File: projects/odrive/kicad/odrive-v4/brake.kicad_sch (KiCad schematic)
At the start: 29 parts, among them J13 BRAKE_EXT, Q50 NVMFS5C628NL/BSC027N10NS5, Q51 NVMFS5C628NL/BSC027N10NS5, U50 UCC27517A, U51 INA181A2, U52 TLV7031, U53 74LVC1G74, U54 74LVC1G32, U55 74LVC1G08

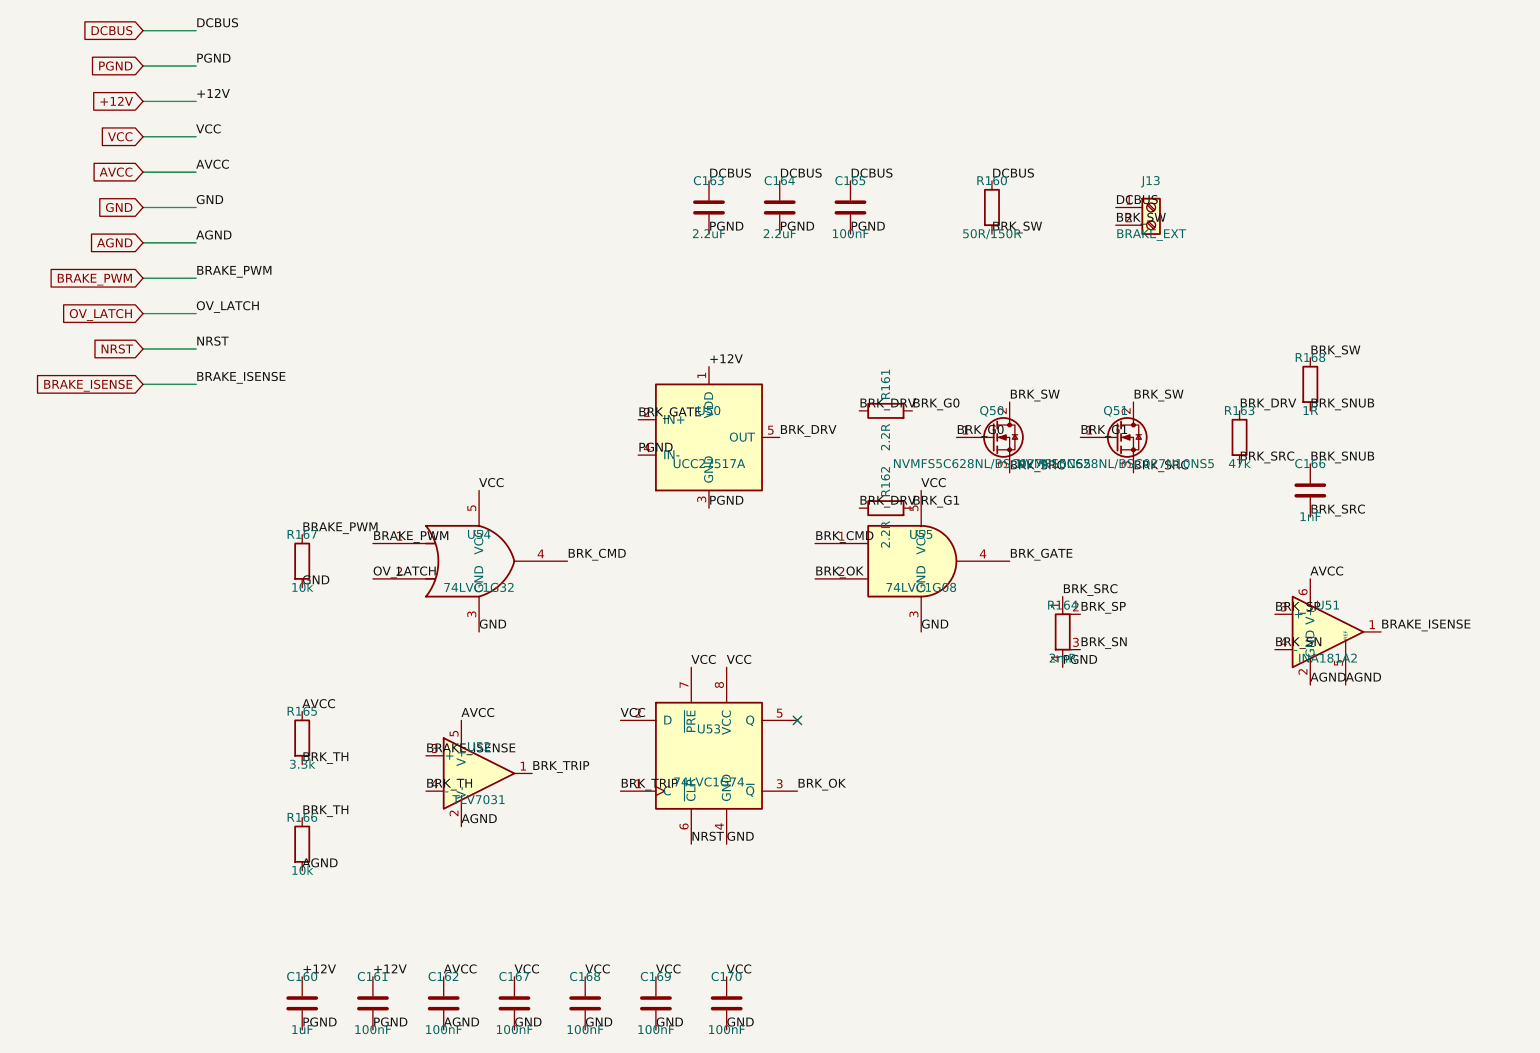
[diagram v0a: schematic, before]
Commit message: Make the v4 schematic sheets readable, netlist-invariant
The verified v4 schematic was electrically perfect and visually unreadable:
connectivity lived in labels stuck on pins, text overlapped, and parts sat
on the title block. Reworked all ten block sheets through Konnect: real
wires for local connections, labels kept for power rails and inter-sheet
nets, parts grouped by function, junction dots where wires join.

The invariant was enforced, not assumed: the exported netlist is diffed
against a reference frozen before the rework - 378 components and 283 nets,
identical membership pin by pin - and ERC holds at 0 errors. The lesson
that forced the rework is now a standing gate: numeric oracles (ERC,
netlist diff, overlap counts) all passed on the unreadable version, so
every sheet is also rendered to PNG and looked at before being declared
done.

An interrupted fix round left one known cosmetic issue, documented in
docs/LOG.md: the encoders-gpio GPIO group's reference/value text fields
float ~134mm right of their symbols, over the title block. konnect 0.2.2
has no tool that repositions property fields, so it waits for 0.11.0.
Also adds the fab footprints the sheets reference (MEGA fuse, Phoenix
terminal blocks, CMC) and restores the board file to the blank template -
the aborted layout skeleton was not worth keeping.
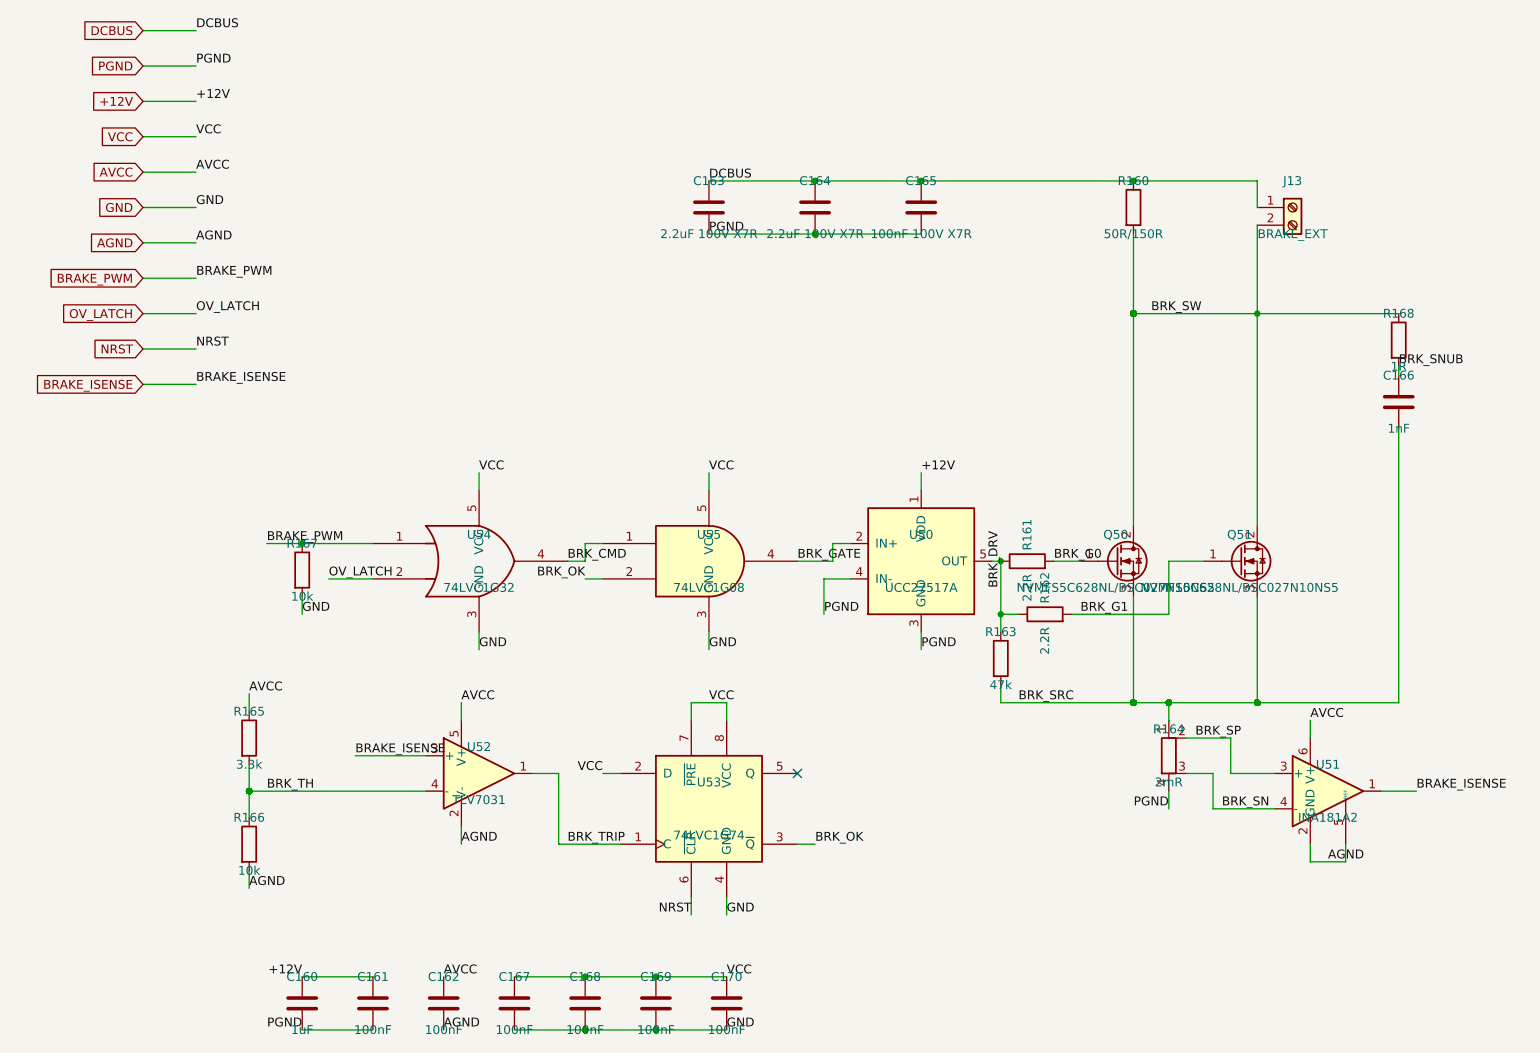
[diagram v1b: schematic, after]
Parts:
- C160, C161, C162, C166, C167, C168, C169, C170: footprint (none) -> Capacitor_SMD:C_0603_1608Metric
- C163, C164: value 2.2uF -> 2.2uF 100V X7R; footprint (none) -> Capacitor_SMD:C_1210_3225Metric
- C165: value 100nF -> 100nF 100V X7R; footprint (none) -> Capacitor_SMD:C_0603_1608Metric
- J13: footprint (none) -> odrive_footprints:TerminalBlock_Phoenix_PC-16-2-ST-10.16mm
- Q50, Q51: footprint (none) -> Package_SO:PowerPAK_SO-8_Single
- R160: footprint (none) -> Resistor_SMD:R_2512_6332Metric
- R161, R162, R163, R165, R166, R167, R168: footprint (none) -> Resistor_SMD:R_0603_1608Metric
- R164: footprint (none) -> Resistor_SMD:R_Shunt_Vishay_WSK2512_6332Metric_T1_T2
- U50, U52, U54, U55: footprint (none) -> Package_TO_SOT_SMD:SOT-23-5
- U51: footprint (none) -> Package_TO_SOT_SMD:SOT-23-6
- U53: footprint (none) -> Package_SO:VSSOP-8_2.4x2.1mm_P0.5mm
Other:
- moved on the sheet: C164, C165, C166, J13, Q50, Q51, R160, R161, R162, R163, R164, R165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

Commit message: Import the v4 netlist onto a 4-layer board, checkpoint before placement
update_pcb_from_schematic (konnect 0.11.0, live IPC, single undo commit)
lands all 378 footprints with 283 nets and zero conflicts. Getting there
took three tries worth of fixes, all kept: the project fp-lib-table now
registers the 18 standard footprint libraries the sheets reference (the
kicad wrapper's KICAD10_FOOTPRINT_DIR is invisible to project resolution,
same story as the symbol libraries); the seven current shunts move to the
real R_Shunt_Vishay_WSK2512_6332Metric_T2.66mm kelvin footprint (the
T1_T2 name the builder invented does not exist); the OV-latch 74LVC1G74
moves to TSSOP-8 (no DCU footprint in this library snapshot - order the
DCT variant); and the SO3 solder jumpers drop the RoundedPad variant
whose custom-shape pads KiCad 10's typed IPC placement path refuses.
Board outline 120x80mm rounded, In1/In2.Cu added file-based after
learning that adding them with pcbnew open gets clobbered by its next
save. Placement not started - components sit stacked at the import
default.
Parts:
- R164: footprint Resistor_SMD:R_Shunt_Vishay_WSK2512_6332Metric_T1_T2 -> Resistor_SMD:R_Shunt_Vishay_WSK2512_6332Metric_T2.66mm
- U53: footprint Package_SO:VSSOP-8_2.4x2.1mm_P0.5mm -> Package_SO:TSSOP-8_3x3mm_P0.65mm
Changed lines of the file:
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@@
         (font
           (size 1.27 1.27))))
-    (property "Footprint" "Resistor_SMD:R_Shunt_Vishay_WSK2512_6332Metric_T1_T2"
+    (property "Footprint" "Resistor_SMD:R_Shunt_Vishay_WSK2512_6332Metric_T2.66mm"
       (at 162.56 124.46 0)
       (hide yes)
@@
         (font
           (size 1.27 1.27))))
-    (property "Footprint" "Package_SO:VSSOP-8_2.4x2.1mm_P0.5mm"
+    (property "Footprint" "Package_SO:TSSOP-8_3x3mm_P0.65mm"
       (at 96.52 132.08 0)
       (hide yes)
